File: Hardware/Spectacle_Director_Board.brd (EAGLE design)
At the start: 27.9 x 58.9 mm, 72 parts, among them Q1 2.5A/30V, Q2 MBT3904DW1T1, U1 MCP73831, U3 AP2112K-3.3V, U4 FT231XS, U5 W25Q32FVSS, Y1 26MHz, Y2 32.768kHz

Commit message: Initial commit of finished layout
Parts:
- removed C14, C16: 0.1uF, SparkFun-Capacitors:0603-CAP
- removed C15, C19: 4.7uF, SparkFun-Capacitors:0603-CAP
- removed J2: (no value), SparkFun-Connectors:MOLEX-1X4_LOCK
- removed JP3: (no value), SparkFun-Passives:PAD-JUMPER-3-3OF3_NC_BY_TRACE_YES_SILK_FULL_BOX
- removed Q1: 2.5A/30V, SparkFun-DiscreteSemi:SOT23-3
- removed R10, R11, R12: 4.7K, SparkFun-Resistors:0603-RES
- removed R13, R14: 27, SparkFun-Resistors:0603-RES
- removed R7: 10K, SparkFun-Resistors:0603-RES@1
- removed SJ1, SJ2: JUMPER-PAD-2-NC_BY_TRACE, SparkFun-Passives:PAD-JUMPER-2-NC_BY_TRACE_YES_SILK
- removed SJ3: (no value), SparkFun-Passives:PAD-JUMPER-3-2OF3_NC_BY_TRACE_YES_SILK_FULL_BOX
- removed U4: FT231XS, SparkFun-DigitalIC:SSOP20_L
- added C2: 1.0uF, SparkFun-Capacitors:0603-CAP
- added D5: PESD1CAN, SparkFun-DiscreteSemi:SOT23-3
- added FD1, FD2, FD3, FD4: FIDUCIALUFIDUCIAL, SparkFun-Aesthetics:MICRO-FIDUCIAL
- added H1, H2, H3, H4: STAND-OFF, SparkFun-Electromechanical:STAND-OFF
- added J4: AUDIO-JACK3, SparkFun-Connectors:AUDIO-JACK-TRRS-SMD
- added U$2: FOUR_LAYER_WARNING, SparkFun-Aesthetics:FOUR_LAYER_WARNING
- C11: value 0.1uF -> 4.7uF; device SparkFun-Capacitors:0603-CAP -> SparkFun-Capacitors:1206-CAP
- C12: value 47pF -> 0.1uF
- C13: value 47pF -> 4.7uF; device SparkFun-Capacitors:0603-CAP -> SparkFun-Capacitors:1206-CAP
- C18, C20, C21, C23, C25: device SparkFun-Capacitors:0603-CAP -> SparkFun-Capacitors:0402-CAP
- C6: value 4.7uF -> 0.1uF
- D1: value Yellow -> PESD1CAN; device SparkFun-LED:LED-0603 -> SparkFun-DiscreteSemi:SOT23-3
- D2: value BAT20J -> PESD1CAN; device SparkFun-DiscreteSemi:SOD-323 -> SparkFun-DiscreteSemi:SOT23-3
- J1: value (none) -> AUDIO-JACK3; device SparkFun-Connectors:MOLEX-1X4_LOCK -> SparkFun-Connectors:AUDIO-JACK-TRRS-SMD
- JP1: value (none) -> JUMPER-PAD-3-NC_BY_PASTE; device SparkFun-Passives:PAD-JUMPER-3-3OF3_NC_BY_TRACE_YES_SILK_FULL_BOX -> SparkFun-Passives:PAD-JUMPER-3-NC_BY_PASTE_YES_SILK_FULL_BOX
- JP2: value LiPo -> JUMPER-PAD-3-NC_BY_PASTE; device SparkFun-Connectors:JST-2-PTH -> SparkFun-Passives:PAD-JUMPER-3-NC_BY_PASTE_YES_SILK_FULL_BOX
- R3: value 1K -> 2.2k
- R5: value DNP -> 2.2k; device SparkFun-Passives:1/6W-RES -> SparkFun-Resistors:0603-RES
- R6: value 2.0k -> 2.2k
- R9: value 4.7K -> 2.2k
- U1: value MCP73831 -> CY7C65213; device SparkFun-PowerIC:SOT23-5 -> SparkFun-DigitalIC:SSOP28DB
- moved R15 62.8 mm to (3.81, 27.3), flipped to the bottom, turned to 90 degrees
- moved R9 27.9 mm to (6.99, 13.6), flipped to the bottom, turned to 90 degrees
- moved R17 24.9 mm to (1.27, 35.6), turned to 270 degrees
- moved LOGO2 24.7 mm to (21.8, 38.6)
- moved S2 23.1 mm to (3.81, 27.3), turned to 0 degrees
- moved R3 21.7 mm to (1.91, 22.9), flipped to the bottom, turned to 90 degrees
- moved Q2 20.8 mm to (3.81, 35.6), turned to 90 degrees
- moved D1 20.5 mm to (4.70, 19.7), flipped to the bottom
- moved D3 20.3 mm to (23.1, 19.9)
- moved R4 20.0 mm to (23.1, 23.1)
- moved C12 18.7 mm to (22.0, 20.2), flipped to the bottom, turned to 0 degrees
- moved J1 18.4 mm to (0.00, 10.2), turned to 0 degrees
- moved R18 18.1 mm to (6.60, 35.6), turned to 270 degrees
- moved JP1 18.1 mm to (4.32, 23.7), turned to 0 degrees
- moved JP2 16.7 mm to (4.70, 14.5), flipped to the bottom, turned to 0 degrees
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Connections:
- removed net 3.3V_F: C16.1, U4.13, U4.14, U4.3
- removed net D+: C13.1, JP15.D+, R14.1
- removed net D-: C12.1, JP15.D-, R13.1
- removed net I2C_SCL_A: J1.4, R10.1, U$1.15
- removed net I2C_SDA_B: J1.3, R9.1
- removed net N$11: JP1.1, R10.2
- removed net N$14: R5.2, SJ1.2, U1.5
- removed net N$16: R6.2, SJ1.1
- removed net N$17: D1.A, R3.2
- removed net N$9: D1.C, U1.1
- removed net VCC_FLASH: C17.1, SJ3.2, U5.8
- removed net VIN: C7.1, D2.C, J1.2, J2.2, Q1.2, U3.1, U3.3
- removed net V_BATT: C6.1, JP2.2, Q1.3, U1.3
- new net GND18: U1.18
- new net GND21: U1.21
- new net GND7: U1.7
- new net I2C_SCL_0: D5.1, J1.RING2, R6.1, U$1.15
- new net NC1: U1.25
- new net VDD: C2.1, U1.17
- net 0: no longer S2.4
- net 3.3V: now also C12.1, C13.1, C17.1, JP2.2, R4.1, U1.4, U5.8; no longer JP3.2, SJ2.2, SJ3.3
- net CHIP_PU: no longer S1.4
- net DTR: now also U1.2; no longer U4.1
- net FLASH_VDD: no longer SJ3.1
- net GND: now also C2.2, D1.3, D2.3, D5.3, J1.TIP, J4.TIP; no longer C14.2, C15.2, C16.2, C19.2, J1.1, J2.1, JP2.1, R5.1, R6.1, R7.1, S1.2, S2.2, U1.2, U4.16, U4.6
- net I2C_SCL_1: now also D1.1, J4.RING2, R3.1; no longer J2.4, R12.1
- net I2C_SDA_0: now also D5.2, J1.RING1, R9.1
- net I2C_SDA_1: now also D1.2, J4.RING1, R5.1; no longer J2.3, R11.1
- net N$3: now also JP1.3, R3.2; no longer R4.1, SJ2.1
- net N$4: now also JP2.3, R6.2; no longer JP3.3, R11.2
- net N$5: now also JP2.1, R9.2; no longer JP3.1, R12.2
- net N$6: now also JP1.1, R5.2; no longer JP1.3, R9.2
- net N$7: now also JP15.D-, U1.16; no longer R13.2, U4.12
- net N$8: now also JP15.D+, U1.15; no longer R14.2, U4.11
- net RTS: now also U1.11; no longer U4.2
- net U0RXD: no longer U4.20
- net U0TXD: now also U1.5; no longer U4.4
- net VUSB: no longer C11.1
- net V_USB: now also C11.1, C6.1, C7.1, D2.1, J1.EARTH, J4.EARTH, U1.20, U3.1, U3.3; no longer C14.1, C15.1, C19.1, D2.A, Q1.1, R3.1, R7.2, U1.4, U4.15
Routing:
- net 3.3V: track 139.7 -> 38.6 mm, vias 8 -> 12
- net 0: track 66.8 -> 12.8 mm
- net RTS: track 6.80 -> 55.0 mm, vias 0 -> 1
- net CHIP_PU: track 59.9 -> 16.9 mm, vias 6 -> 0
- net DTR: track 11.4 -> 50.1 mm
- net VIN: track 36.2 -> 0.00 mm
- net U0RXD: track 32.8 -> 0.00 mm, vias 2 -> 0
- net I2C_SCL_0: track 0.00 -> 28.7 mm, vias 0 -> 3
- net I2C_SDA_0: track 2.03 -> 25.2 mm, vias 0 -> 3
- net I2C_SDA_1: track 29.4 -> 11.8 mm
- net I2C_SCL_A: track 16.7 -> 0.00 mm, vias 2 -> 0
- net V_BATT: track 13.7 -> 0.00 mm, vias 3 -> 0
- net N$9: track 13.5 -> 0.00 mm, vias 2 -> 0
- net 3.3V_F: track 13.5 -> 0.00 mm
- net N$8: track 17.5 -> 4.40 mm, vias 2 -> 1
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- added copper zone on layer 15, net 3.3V
- added copper zone on layer 2, net GND
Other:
- board size 27.9 x 58.9 mm -> 25.4 x 55.9 mm
- board text added: "Mike Hord"
- board text added: "Spectacle\! Director Board"
- board text removed: "0"
- board text removed: "CHL A"
- board text removed: "CHL B"
- board text removed: "Director Board"
- board text removed: "Jim Lindblom"
- board text removed: "RST"
- board text removed: "SJ1"
- board text removed: "SJ2"
- board text removed: "SJ3"
- board text removed: "Spectacle!"

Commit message: For QC review
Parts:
- C26, C9: value (none) -> 22pF; device SparkFun-Passives:0603-CAP -> SparkFun-Capacitors:0603-CAP
- moved E1 0.25 mm to (11.2, 43.6)
- moved LOGO1 0.25 mm to (1.78, 43.3)
- moved R9 0.13 mm to (7.11, 13.6)
- renumbered U$1 to U4
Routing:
- net GND: vias 50 -> 70
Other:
- board text added: "A"
- board text added: "B"

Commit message: Feedback from QC review
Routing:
- net 3.3V: track 38.6 -> 39.6 mm
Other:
- board text added: "1"
- board text added: "2"
- board text added: "3"
- board text added: "4"
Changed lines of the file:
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@@
 <layers>
 <layer number="1" name="Top" color="4" fill="1" visible="yes" active="yes"/>
-<layer number="2" name="Route2" color="1" fill="3" visible="no" active="yes"/>
-<layer number="15" name="Route15" color="4" fill="6" visible="no" active="yes"/>
+<layer number="2" name="Route2" color="1" fill="3" visible="yes" active="yes"/>
+<layer number="15" name="Route15" color="4" fill="6" visible="yes" active="yes"/>
 <layer number="16" name="Bottom" color="1" fill="1" visible="yes" active="yes"/>
 <layer number="17" name="Pads" color="2" fill="1" visible="yes" active="yes"/>
@@
 <layer number="20" name="Dimension" color="15" fill="1" visible="yes" active="yes"/>
 <layer number="21" name="tPlace" color="16" fill="1" visible="yes" active="yes"/>
-<layer number="22" name="bPlace" color="14" fill="1" visible="no" active="yes"/>
+<layer number="22" name="bPlace" color="14" fill="1" visible="yes" active="yes"/>
 <layer number="23" name="tOrigins" color="15" fill="1" visible="yes" active="yes"/>
-<layer number="24" name="bOrigins" color="15" fill="1" visible="no" active="yes"/>
-<layer number="25" name="tNames" color="7" fill="1" visible="yes" active="yes"/>
+<layer number="24" name="bOrigins" color="15" fill="1" visible="yes" active="yes"/>
+<layer number="25" name="tNames" color="7" fill="1" visible="no" active="yes"/>
 <layer number="26" name="bNames" color="7" fill="1" visible="no" active="yes"/>
 <layer number="27" name="tValues" color="7" fill="1" visible="no" active="yes"/>
@@
 <layer number="39" name="tKeepout" color="16" fill="11" visible="no" active="yes"/>
 <layer number="40" name="bKeepout" color="1" fill="11" visible="no" active="yes"/>
-<layer number="41" name="tRestrict" color="4" fill="10" visible="no" active="yes"/>
+<layer number="41" name="tRestrict" color="4" fill="10" visible="yes" active="yes"/>
 <layer number="42" name="bRestrict" color="1" fill="10" visible="no" active="yes"/>
 <layer number="43" name="vRestrict" color="2" fill="10" visible="no" active="yes"/>
 <layer number="44" name="Drills" color="7" fill="1" visible="no" active="yes"/>
-<layer number="45" name="Holes" color="7" fill="1" visible="no" active="yes"/>
+<layer number="45" name="Holes" color="7" fill="1" visible="yes" active="yes"/>
 <layer number="46" name="Milling" color="3" fill="1" visible="no" active="yes"/>
 <layer number="47" name="Measures" color="7" fill="1" visible="no" active="yes"/>
-<layer number="51" name="tDocu" color="6" fill="1" visible="no" active="yes"/>
+<layer number="51" name="tDocu" color="6" fill="1" visible="yes" active="yes"/>
 <layer number="52" name="bDocu" color="7" fill="1" visible="no" active="yes"/>
 <layer number="3" name="Route3" color="4" fill="3" visible="no" active="no"/>
@@
 <dimension x1="25.4" y1="53.34" x2="25.4" y2="55.88" x3="29.21" y3="54.61" textsize="1.27" textratio="15" layer="47" dtype="vertical" unit="inch"/>
 <dimension x1="22.86" y1="55.88" x2="25.4" y2="55.88" x3="24.13" y3="63.5" textsize="1.27" textratio="15" layer="47" dtype="horizontal" unit="inch"/>
+<text x="23.495" y="5.08" size="0.8128" layer="1" font="vector" ratio="15">1</text>
+<text x="24.13" y="5.08" size="0.8128" layer="2" font="vector" ratio="15">2</text>
+<text x="23.495" y="4.191" size="0.8128" layer="15" font="vector" ratio="15">3</text>
+<text x="24.765" y="4.191" size="0.8128" layer="16" font="vector" ratio="15" rot="MR0">4</text>
+<rectangle x1="11.811" y1="32.004" x2="12.319" y2="32.258" layer="41"/>
+<rectangle x1="14.224" y1="29.591" x2="14.478" y2="30.099" layer="41"/>
+<rectangle x1="11.811" y1="27.432" x2="12.319" y2="27.686" layer="41"/>
+<rectangle x1="9.652" y1="29.591" x2="9.906" y2="30.099" layer="41"/>
 </plain>
 <attributes>
@@
 <attribute name="PROD_ID" value="CAP-00867" x="17.907" y="33.147" size="1.778" layer="27" font="vector" ratio="15" rot="R270" display="off"/>
 </element>
-<element name="R2" library="SparkFun-Passives" package="0603-RES" value="14k" x="19.304" y="33.147" rot="R270"/>
+<element name="R2" library="SparkFun-Passives" package="0603-RES" value="14k" x="19.304" y="33.147" rot="R270">
+<attribute name="PROD_ID" value="RES-13340" x="19.304" y="33.147" size="1.778" layer="27" rot="R270" display="off"/>
+</element>
 <element name="U5" library="SparkFun-DigitalIC" package="SOIC-8" value="W25Q32FVSS" x="19.05" y="17.78">
 <attribute name="PROD_ID" value="IC-13229" x="11.43" y="27.94" size="1.778" layer="27" font="vector" ratio="15" display="off"/>
@@
 <wire x1="15.93" y1="32.766" x2="14.986" y2="32.766" width="0.2032" layer="16"/>
 <via x="14.986" y="32.766" extent="1-16" drill="0.254"/>
-<wire x1="14.265" y1="32.795" x2="14.294" y2="32.766" width="0.2032" layer="1"/>
-<wire x1="14.294" y1="32.766" x2="14.986" y2="32.766" width="0.2032" layer="1"/>
 <via x="16.764" y="30.988" extent="1-16" drill="0.254"/>
 <wire x1="15.015" y1="31.245" x2="16.507" y2="31.245" width="0.2032" layer="1"/>
@@
 <wire x1="23.114" y1="23.964" x2="23.114" y2="25.019" width="0.2032" layer="1"/>
 <via x="23.114" y="25.019" extent="1-16" drill="0.254"/>
+<wire x1="14.265" y1="32.795" x2="14.265" y2="33.315" width="0.2032" layer="1"/>
+<wire x1="14.265" y1="33.315" x2="14.351" y2="33.401" width="0.2032" layer="1"/>
+<wire x1="14.351" y1="33.401" x2="14.732" y2="33.401" width="0.2032" layer="1"/>
+<wire x1="14.732" y1="33.401" x2="14.859" y2="33.274" width="0.2032" layer="1"/>
+<wire x1="14.859" y1="33.274" x2="14.859" y2="32.893" width="0.2032" layer="1"/>
+<wire x1="14.859" y1="32.893" x2="14.986" y2="32.766" width="0.2032" layer="1"/>
 </signal>
 <signal name="CHIP_PU">

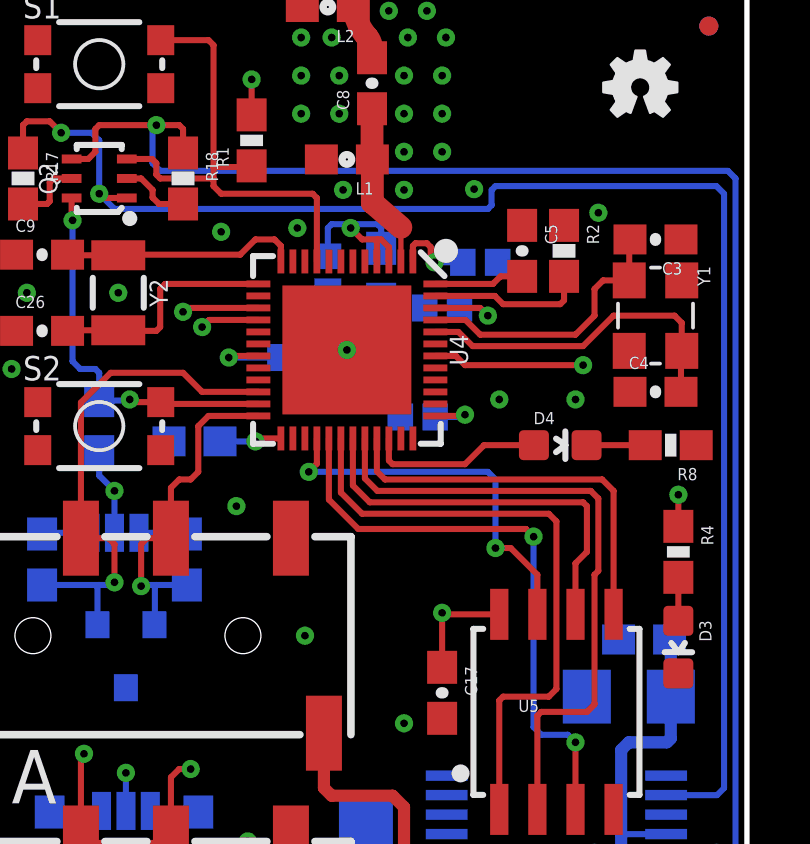
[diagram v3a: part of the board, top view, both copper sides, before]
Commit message: Changes due to Espressif changing chip before release
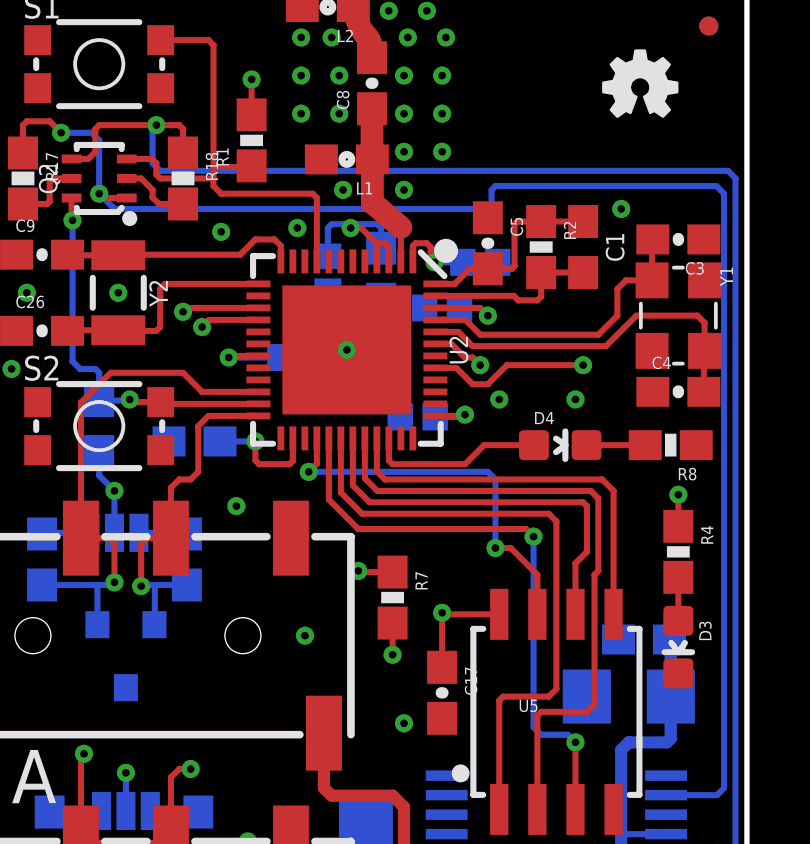
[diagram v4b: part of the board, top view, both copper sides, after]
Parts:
- added C1: 3.0nF, esp32-thing-temp:0603
- added R7: 10K, SparkFun-Resistors:0603-RES
- R2: value 14k -> 20k; device SparkFun-Passives:0603-RES -> SparkFun-Resistors:0603-RES
- U2: value ESP32 -> ESP3212
- moved C5 1.17 mm to (16.8, 33.4)
- moved R2 0.77 mm to (18.5, 33.3)
- moved C3 0.76 mm to (23.1, 33.5)
- moved C4 0.76 mm to (23.1, 28.4)
- moved Y1 0.76 mm to (23.1, 31.0)
- renumbered U4 to U2
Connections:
- removed net RES_14K: R2.2, U2.47
- new net N$11: C1.2, R2.2, U2.47
- net 0: now also R7.1
- net 3.3V: now also R7.2, U2.43
- net CAP_10N: now also C1.1, R2.1
- net FLASH_VDD: now also U2.26; no longer U2.25
- net GND: no longer R2.1
- net U0RXD: now also U2.40; no longer U2.41
- net U0TXD: now also U2.41; no longer U2.42
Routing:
- net 0: track 12.8 -> 27.2 mm, vias 2 -> 3
- net N$11: track 0.00 -> 5.84 mm
- net RES_14K: track 5.26 -> 0.00 mm
- net CAP_10N: track 3.00 -> 6.60 mm
- net 3.3V: track 39.6 -> 42.3 mm, vias 12 -> 14
- net FLASH_VDD: track 2.07 -> 3.92 mm
- net XTAL_P_: track 9.31 -> 10.1 mm
- net XTAL_N_: track 11.2 -> 12.0 mm
- net GND: vias 70 -> 69

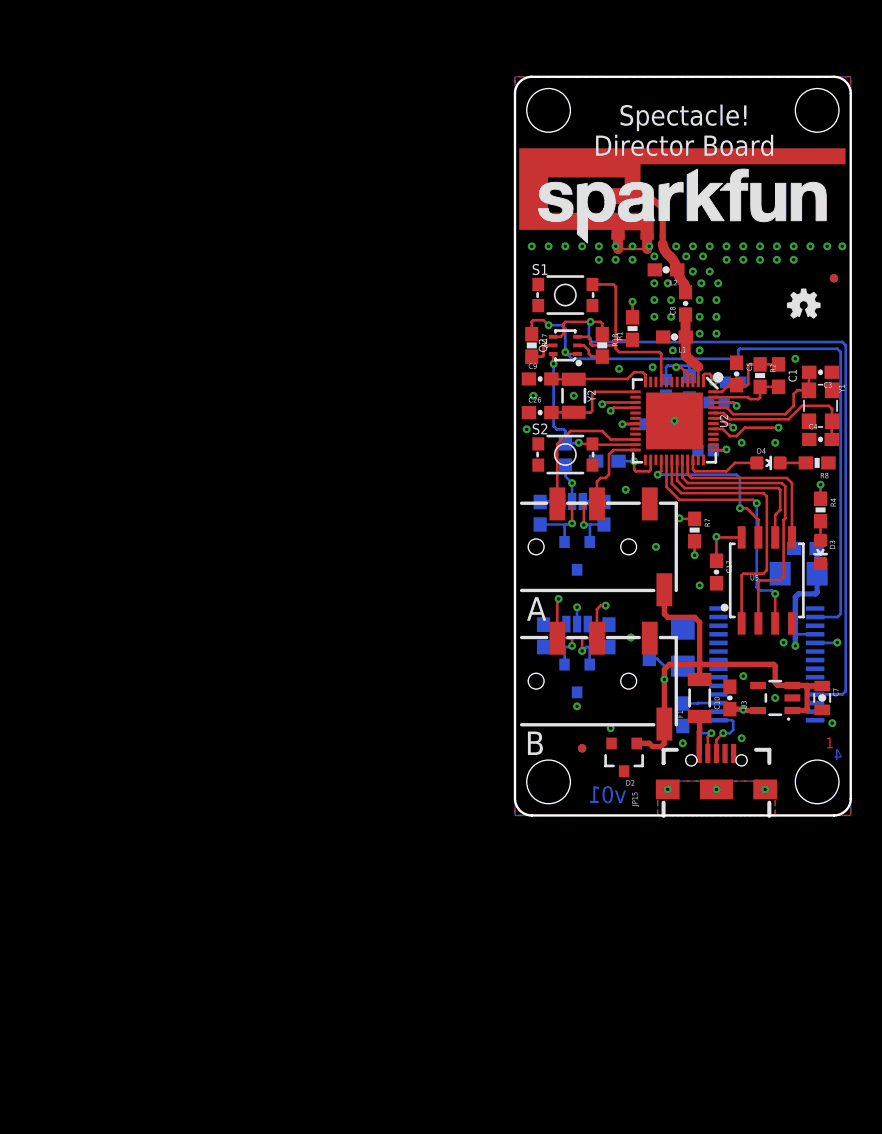
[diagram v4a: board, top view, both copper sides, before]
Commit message: Changes from design review for v02
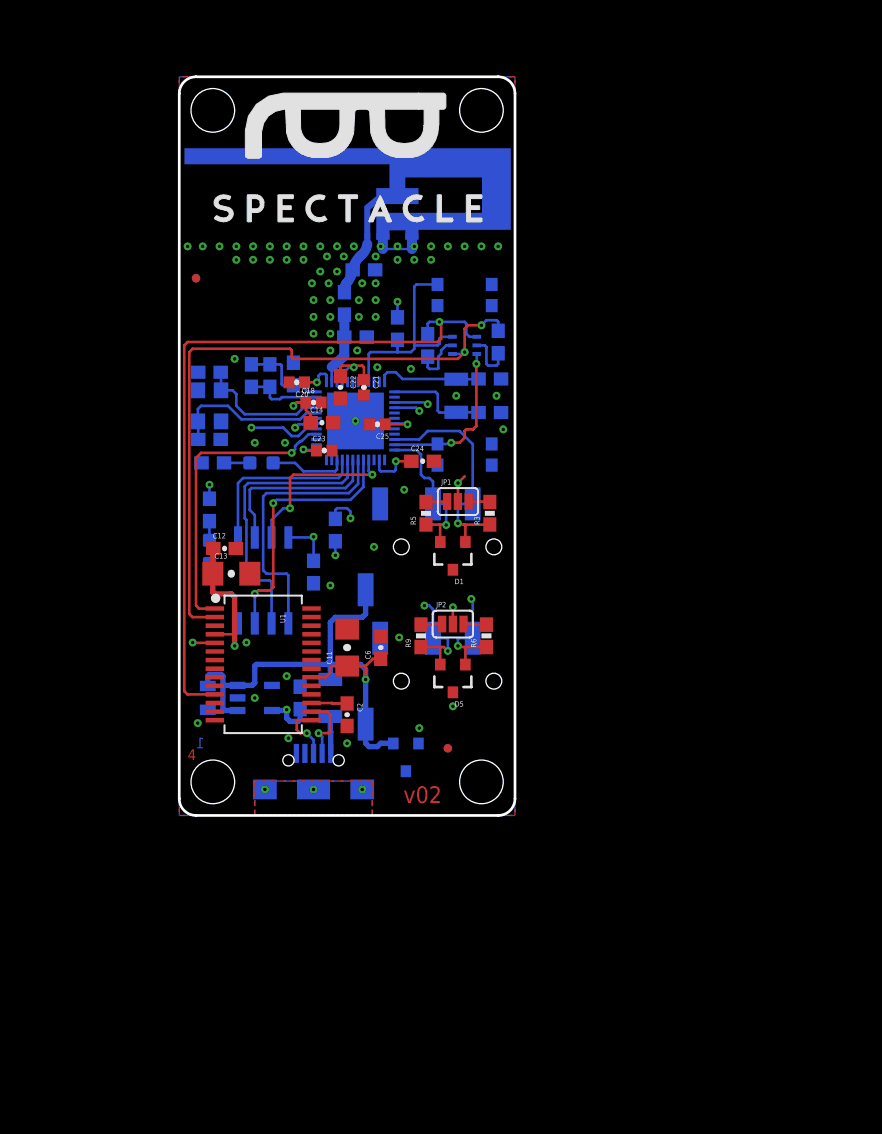
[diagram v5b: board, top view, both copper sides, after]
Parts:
- removed R15: 10K, SparkFun-Resistors:0603-RES@1
- added C14: 1.0uF, SparkFun-Capacitors:0603-CAP
- moved U$2 73.7 mm to (36.8, -11.4), flipped to the bottom
- moved FD2 48.3 mm to (-24.1, 40.6), flipped to the bottom
- moved FD4 48.3 mm to (-24.1, 40.6), flipped to the top
- moved C7 46.5 mm to (-23.2, 8.89), flipped to the bottom
- moved C3 46.2 mm to (-23.1, 33.5), flipped to the bottom
- moved C4 46.2 mm to (-23.1, 28.4), flipped to the bottom
- moved D3 46.2 mm to (-23.1, 19.9), flipped to the bottom
- moved R4 46.2 mm to (-23.1, 23.1), flipped to the bottom
- moved Y1 46.2 mm to (-23.1, 31.0), flipped to the bottom
- moved H2 45.7 mm to (-22.9, 53.3), flipped to the bottom
- moved H3 45.7 mm to (-22.9, 2.54), flipped to the bottom
- moved R8 45.7 mm to (-22.9, 26.7), flipped to the bottom
- moved C12 43.9 mm to (-22.0, 20.2), flipped to the top
- moved LOGO2 43.7 mm to (-21.8, 38.6), flipped to the bottom
- moved C13 42.9 mm to (-21.5, 18.3), flipped to the top
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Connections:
- net 0: no longer R15.2
- net 3.3V: now also C14.1; no longer R15.1
- net GND: now also C14.2
- net U0RXD: now also U1.1
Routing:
- net U0RXD: track 0.00 -> 22.7 mm, vias 0 -> 1
- net 3.3V: track 42.3 -> 44.9 mm
- net N$12: track 2.37 -> 4.13 mm
- net V_USB: track 40.6 -> 42.1 mm
- net N$10: track 2.34 -> 3.85 mm
- net 0: track 27.2 -> 28.3 mm
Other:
- board text added: "Silkscreen to be WHITE Soldermask to be BLACK"
- board text added: "v02"
- board text removed: "v01"
